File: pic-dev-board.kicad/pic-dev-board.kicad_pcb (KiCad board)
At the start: 2 copper layers, 100 x 100 mm, 80 parts, among them J1 Conn_GP0, J10 Jumper DATin, J11 Conn_SR_2, J12 Conn_SR_1, J13 Conn_5V_GND, J14 Jumper CLKin, J15 Barrel_Jack_Switch, J16 RUN/~PGM, J17 I2C, J18 GP1(RA1)/RB6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

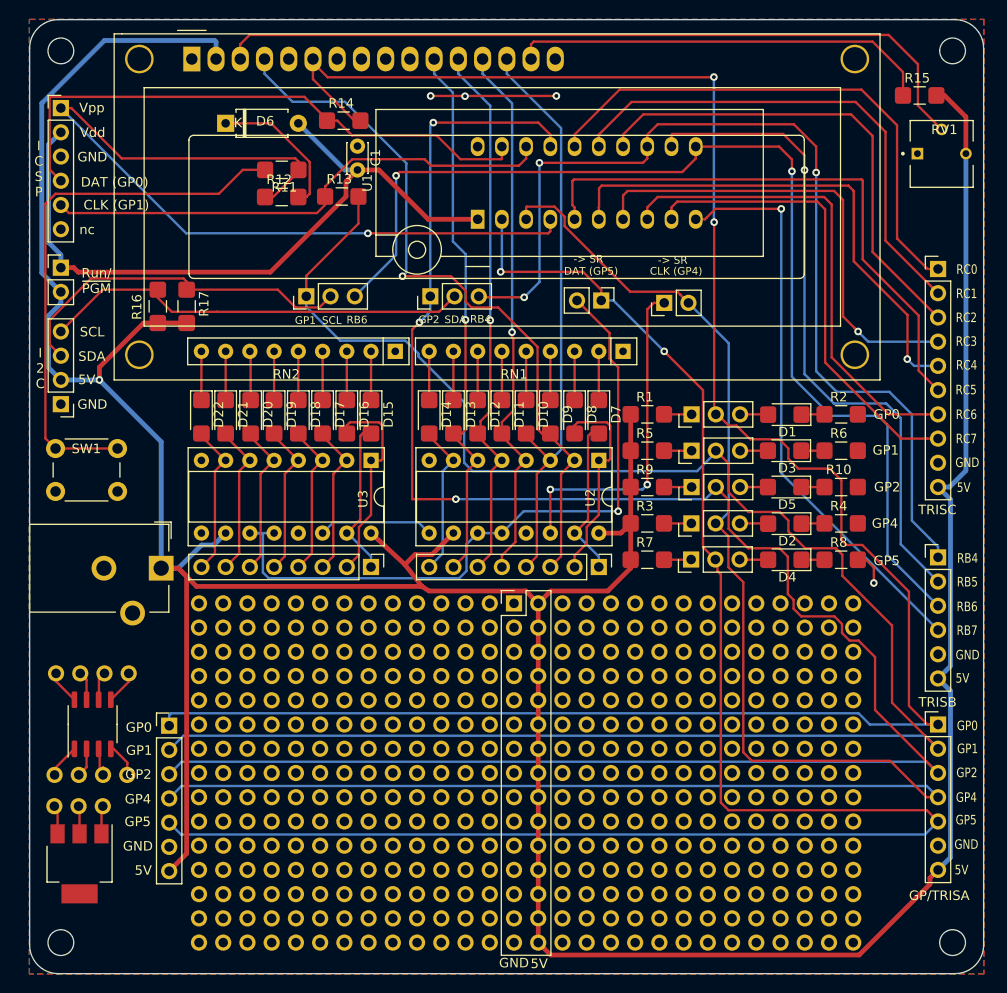
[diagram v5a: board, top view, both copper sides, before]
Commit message: fine-tuning of traces
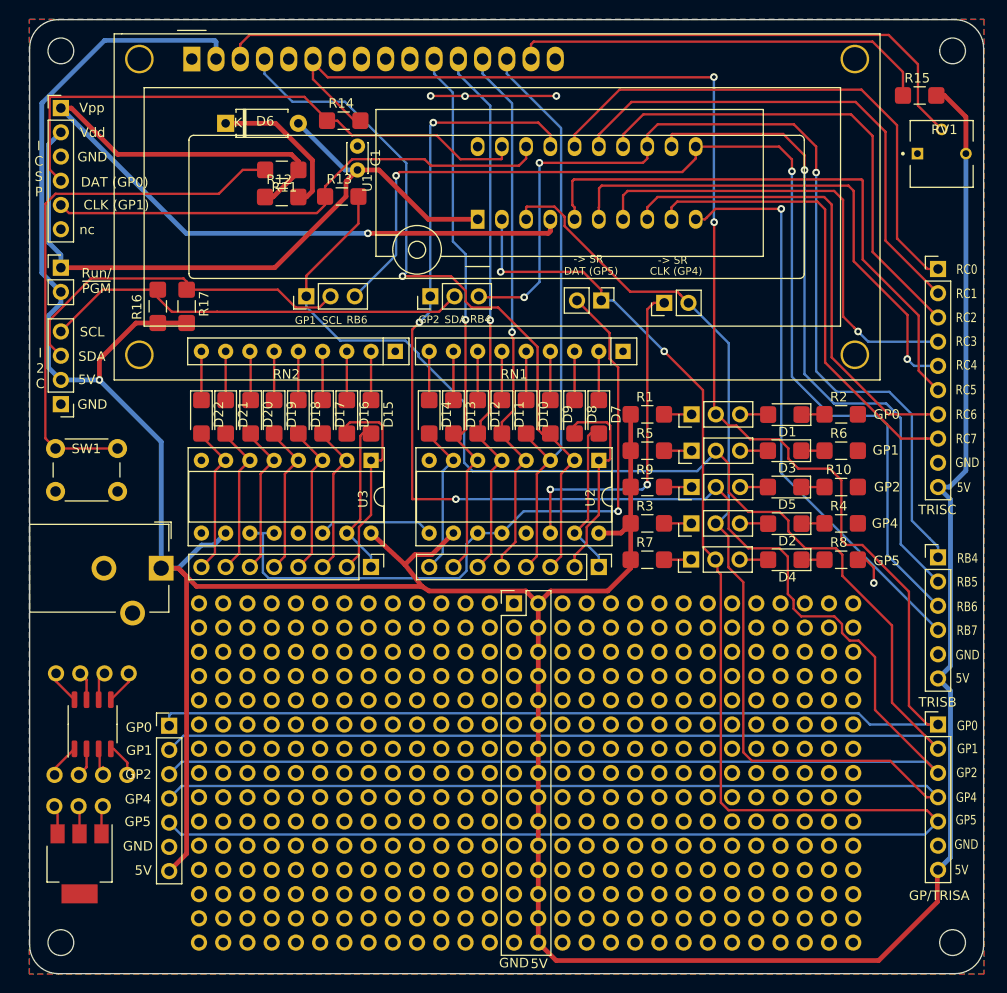
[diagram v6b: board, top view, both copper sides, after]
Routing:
- net +5V: track 389.5 -> 392.0 mm
- net Net-(D6-Pad1): track 15.2 -> 15.7 mm
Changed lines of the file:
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@@
     (thickness 1.6)
     (drawings 73)
-    (tracks 691)
+    (tracks 688)
     (zones 0)
     (modules 80)
@@
     (add_net "Net-(D5-Pad1)")
     (add_net "Net-(D5-Pad2)")
-    (add_net "Net-(D6-Pad1)")
     (add_net "Net-(D7-Pad1)")
     (add_net "Net-(D8-Pad1)")
@@
     (add_net +5V)
     (add_net /Vdd)
+    (add_net "Net-(D6-Pad1)")
   )
   (module Socket:DIP_Socket-20_W4.3_W5.08_W7.62_W10.16_W10.9_3M_220-3342-00-0602J (layer F.Cu)
@@
   (segment (start 31.973999 43.108401) (end 31.973999 53.349999) (width 0.5) (layer B.Cu) (net 1))
   (segment (start 33.274 41.8084) (end 31.973999 43.108401) (width 0.5) (layer B.Cu) (net 1) (status 10))
-  (segment (start 63.16609 46.95371) (end 63.563601 46.556199) (width 0.5) (layer F.Cu) (net 1))
-  (segment (start 34.624 56) (end 35.092001 56.468001) (width 0.5) (layer F.Cu) (net 1))
-  (segment (start 33.274 56) (end 34.624 56) (width 0.5) (layer F.Cu) (net 1))
-  (segment (start 63.563601 46.556199) (end 64.3636 45.7562) (width 0.5) (layer F.Cu) (net 1))
-  (segment (start 55.229639 56.468001) (end 63.16609 48.53155) (width 0.5) (layer F.Cu) (net 1))
-  (segment (start 63.16609 48.53155) (end 63.16609 46.95371) (width 0.5) (layer F.Cu) (net 1))
-  (segment (start 35.092001 56.468001) (end 55.229639 56.468001) (width 0.5) (layer F.Cu) (net 1))
   (segment (start 63.0536 45.7562) (end 64.3636 45.7562) (width 0.5) (layer B.Cu) (net 1))
   (segment (start 58.166 40.8686) (end 63.0536 45.7562) (width 0.5) (layer B.Cu) (net 1))
@@
   (segment (start 64.3636 45.7562) (end 66.6096 45.7562) (width 0.5) (layer F.Cu) (net 1))
   (segment (start 66.6096 45.7562) (end 71.7804 50.927) (width 0.5) (layer F.Cu) (net 1))
+  (segment (start 63.563601 46.556199) (end 64.3636 45.7562) (width 0.5) (layer F.Cu) (net 1))
+  (segment (start 63.16609 46.95371) (end 63.563601 46.556199) (width 0.5) (layer F.Cu) (net 1))
+  (segment (start 63.16609 48.53155) (end 63.16609 46.95371) (width 0.5) (layer F.Cu) (net 1))
+  (segment (start 33.274 56) (end 55.69764 56) (width 0.5) (layer F.Cu) (net 1))
+  (segment (start 55.69764 56) (end 63.16609 48.53155) (width 0.5) (layer F.Cu) (net 1))
   (via (at 118.491 89.0524) (size 0.8) (drill 0.4) (layers F.Cu B.Cu) (net 2))
   (segment (start 118.491 87.4395) (end 118.491 89.0524) (width 0.25) (layer F.Cu) (net 2))
@@
   (segment (start 104.648 78.994) (end 107.2125 78.994) (width 0.25) (layer F.Cu) (net 11) (status 30))
   (segment (start 110.7075 78.994) (end 113.3205 78.994) (width 0.25) (layer F.Cu) (net 12) (status 30))
-  (segment (start 55.313864 40.8686) (end 51.696 40.8686) (width 0.25) (layer F.Cu) (net 13))
-  (segment (start 51.696 40.8686) (end 50.546 40.8686) (width 0.25) (layer F.Cu) (net 13))
-  (segment (start 59.35531 44.910046) (end 55.313864 40.8686) (width 0.25) (layer F.Cu) (net 13))
-  (segment (start 59.35531 48.25179) (end 59.35531 44.910046) (width 0.25) (layer F.Cu) (net 13))
-  (segment (start 59.0169 48.5902) (end 59.35531 48.25179) (width 0.25) (layer F.Cu) (net 13))
-  (segment (start 58.1669 48.5902) (end 59.0169 48.5902) (width 0.25) (layer F.Cu) (net 13))
+  (segment (start 59.0169 48.5902) (end 58.1669 48.5902) (width 0.5) (layer F.Cu) (net 13))
+  (segment (start 59.6392 44.7294) (end 59.6392 47.9679) (width 0.5) (layer F.Cu) (net 13))
+  (segment (start 59.6392 47.9679) (end 59.0169 48.5902) (width 0.5) (layer F.Cu) (net 13))
+  (segment (start 55.7784 40.8686) (end 59.6392 44.7294) (width 0.5) (layer F.Cu) (net 13))
+  (segment (start 50.546 40.8686) (end 55.7784 40.8686) (width 0.5) (layer F.Cu) (net 13))
   (segment (start 88.536999 73.631501) (end 88.787 73.3815) (width 0.25) (layer F.Cu) (net 14) (status 20))
   (segment (start 88.536999 82.405001) (end 88.536999 73.631501) (width 0.25) (layer F.Cu) (net 14))
@@
   (segment (start 126.522001 100.360001) (end 126.522001 117.825999) (width 0.5) (layer B.Cu) (net 53))
   (segment (start 125.222 99.06) (end 126.522001 100.360001) (width 0.5) (layer B.Cu) (net 53) (status 10))
-  (segment (start 84.612001 128.046001) (end 83.312 126.746) (width 0.5) (layer F.Cu) (net 53) (status 20))
-  (segment (start 116.956001 128.046001) (end 84.612001 128.046001) (width 0.5) (layer F.Cu) (net 53))
-  (segment (start 124.372001 120.630001) (end 116.956001 128.046001) (width 0.5) (layer F.Cu) (net 53))
-  (segment (start 124.372001 119.975999) (end 124.372001 120.630001) (width 0.5) (layer F.Cu) (net 53))
-  (segment (start 125.222 119.126) (end 124.372001 119.975999) (width 0.5) (layer F.Cu) (net 53) (status 10))
   (segment (start 83.312 126.746) (end 83.312 124.206) (width 0.5) (layer F.Cu) (net 53) (status 30))
   (segment (start 83.312 124.206) (end 83.312 91.186) (width 0.5) (layer F.Cu) (net 53) (status 30))
@@
   (segment (start 43.7896 74.2442) (end 37.3126 67.7672) (width 0.5) (layer B.Cu) (net 53))
   (via (at 37.3126 67.7672) (size 0.8) (drill 0.4) (layers F.Cu B.Cu) (net 53))
-  (segment (start 37.3126 66.430598) (end 37.3126 67.7672) (width 0.5) (layer F.Cu) (net 53))
-  (segment (start 41.944098 61.7991) (end 37.3126 66.430598) (width 0.5) (layer F.Cu) (net 53))
-  (segment (start 43.434 61.7991) (end 41.944098 61.7991) (width 0.5) (layer F.Cu) (net 53) (status 10))
   (segment (start 43.434 61.7991) (end 46.4566 61.7991) (width 0.5) (layer F.Cu) (net 53) (status 30))
   (segment (start 46.451999 88.365399) (end 45.5896 87.503) (width 0.5) (layer F.Cu) (net 53))
@@
   (segment (start 45.5896 87.503) (end 43.7896 87.503) (width 0.5) (layer F.Cu) (net 53) (status 20))
   (segment (start 44.6278 119.253) (end 46.451999 117.428801) (width 0.5) (layer F.Cu) (net 53) (status 10))
+  (segment (start 37.3126 65.6336) (end 37.3126 67.7672) (width 0.5) (layer F.Cu) (net 53))
+  (segment (start 43.434 61.7991) (end 41.1471 61.7991) (width 0.5) (layer F.Cu) (net 53))
+  (segment (start 41.1471 61.7991) (end 37.3126 65.6336) (width 0.5) (layer F.Cu) (net 53))
+  (segment (start 85.1916 128.6256) (end 83.312 126.746) (width 0.5) (layer F.Cu) (net 53))
+  (segment (start 118.999 128.6256) (end 85.1916 128.6256) (width 0.5) (layer F.Cu) (net 53))
+  (segment (start 125.1458 122.4788) (end 118.999 128.6256) (width 0.5) (layer F.Cu) (net 53))
+  (segment (start 125.222 119.126) (end 125.1458 119.2022) (width 0.5) (layer F.Cu) (net 53))
+  (segment (start 125.1458 119.2022) (end 125.1458 122.4788) (width 0.5) (layer F.Cu) (net 53))
   (segment (start 99.568 71.374) (end 96.4955 71.374) (width 0.25) (layer F.Cu) (net 54) (status 30))
   (segment (start 105.702998 107.696) (end 104.807001 106.800003) (width 0.25) (layer F.Cu) (net 55))
@@
   (segment (start 33.274 46.8884) (end 32.098999 45.713399) (width 0.25) (layer F.Cu) (net 65))
   (segment (start 79.42699 44.63201) (end 79.502 44.557) (width 0.25) (layer F.Cu) (net 65))
-  (segment (start 58.1803 45.9318) (end 58.1803 45.7454) (width 0.25) (layer F.Cu) (net 66))
-  (segment (start 55.5219 48.5902) (end 58.1803 45.9318) (width 0.25) (layer F.Cu) (net 66))
-  (segment (start 54.6719 48.5902) (end 55.5219 48.5902) (width 0.25) (layer F.Cu) (net 66))
-  (segment (start 58.1803 44.8704) (end 58.1803 45.7454) (width 0.25) (layer F.Cu) (net 66))
-  (segment (start 34.374 39.2684) (end 39.65099 44.54539) (width 0.25) (layer F.Cu) (net 66))
-  (segment (start 57.85529 44.54539) (end 58.1803 44.8704) (width 0.25) (layer F.Cu) (net 66))
-  (segment (start 39.65099 44.54539) (end 57.85529 44.54539) (width 0.25) (layer F.Cu) (net 66))
-  (segment (start 33.274 39.2684) (end 34.374 39.2684) (width 0.25) (layer F.Cu) (net 66))
-  (segment (start 84.3588 52.4002) (end 65.4558 52.4002) (width 0.25) (layer F.Cu) (net 66))
-  (segment (start 84.582 50.927) (end 84.582 52.177) (width 0.25) (layer F.Cu) (net 66))
+  (segment (start 58.1803 45.9318) (end 58.1803 45.7454) (width 0.5) (layer F.Cu) (net 66))
+  (segment (start 55.5219 48.5902) (end 58.1803 45.9318) (width 0.5) (layer F.Cu) (net 66))
+  (segment (start 54.6719 48.5902) (end 55.5219 48.5902) (width 0.5) (layer F.Cu) (net 66))
+  (segment (start 84.3588 52.4002) (end 65.4558 52.4002) (width 0.5) (layer F.Cu) (net 66))
+  (segment (start 84.582 50.927) (end 84.582 52.177) (width 0.5) (layer F.Cu) (net 66))
   (via (at 65.4558 52.4002) (size 0.8) (drill 0.4) (layers F.Cu B.Cu) (net 66))
-  (segment (start 84.582 52.177) (end 84.3588 52.4002) (width 0.25) (layer F.Cu) (net 66))
-  (segment (start 46.4058 52.4002) (end 33.274 39.2684) (width 0.25) (layer B.Cu) (net 66))
-  (segment (start 65.4558 52.4002) (end 46.4058 52.4002) (width 0.25) (layer B.Cu) (net 66))
+  (segment (start 84.582 52.177) (end 84.3588 52.4002) (width 0.5) (layer F.Cu) (net 66))
+  (segment (start 46.4058 52.4002) (end 33.274 39.2684) (width 0.5) (layer B.Cu) (net 66))
+  (segment (start 65.4558 52.4002) (end 46.4058 52.4002) (width 0.5) (layer B.Cu) (net 66))
+  (segment (start 57.4297 44.1198) (end 58.1803 44.8704) (width 0.5) (layer F.Cu) (net 66))
+  (segment (start 58.1803 44.8704) (end 58.1803 45.7454) (width 0.5) (layer F.Cu) (net 66))
+  (segment (start 39.2254 44.1198) (end 57.4297 44.1198) (width 0.5) (layer F.Cu) (net 66))
+  (segment (start 33.274 39.2684) (end 34.374 39.2684) (width 0.5) (layer F.Cu) (net 66))
+  (segment (start 34.374 39.2684) (end 39.2254 44.1198) (width 0.5) (layer F.Cu) (net 66))
   (segment (start 124.019919 73.914) (end 125.222 73.914) (width 0.25) (layer F.Cu) (net 67))
   (segment (start 121.365864 73.914) (end 124.019919 73.914) (width 0.25) (layer F.Cu) (net 67))

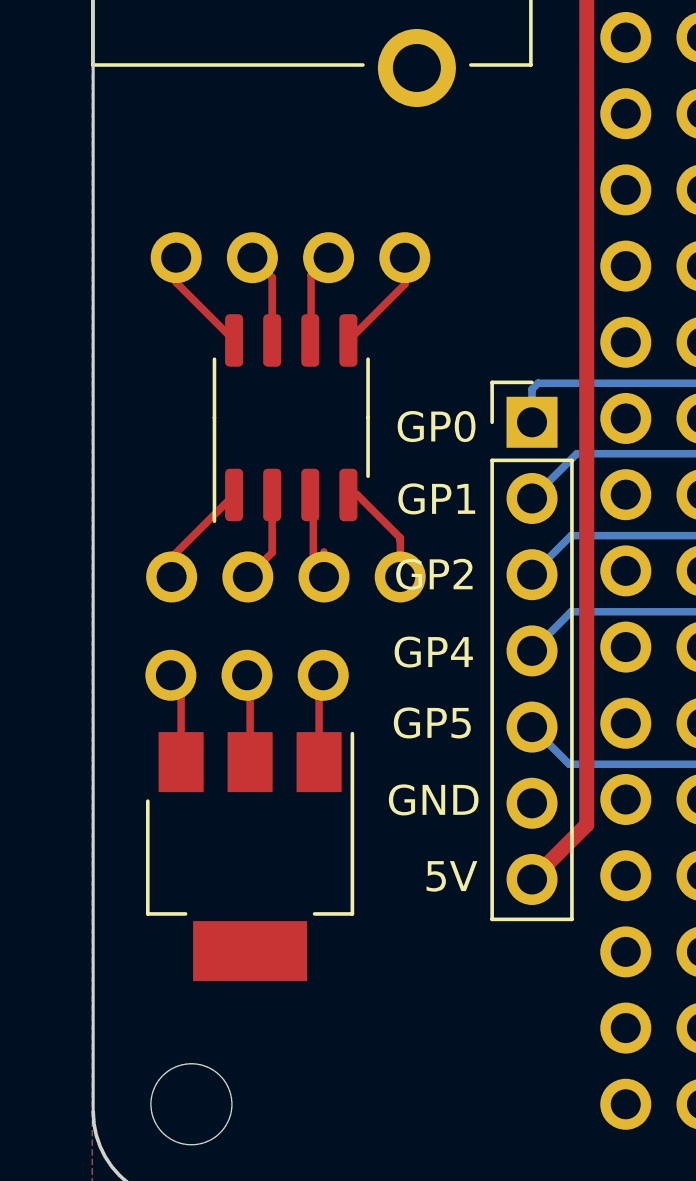
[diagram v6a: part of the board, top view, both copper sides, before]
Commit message: Rev4: added SO-8/SOT-223 components to schema to prevent DRC-errors on pcb
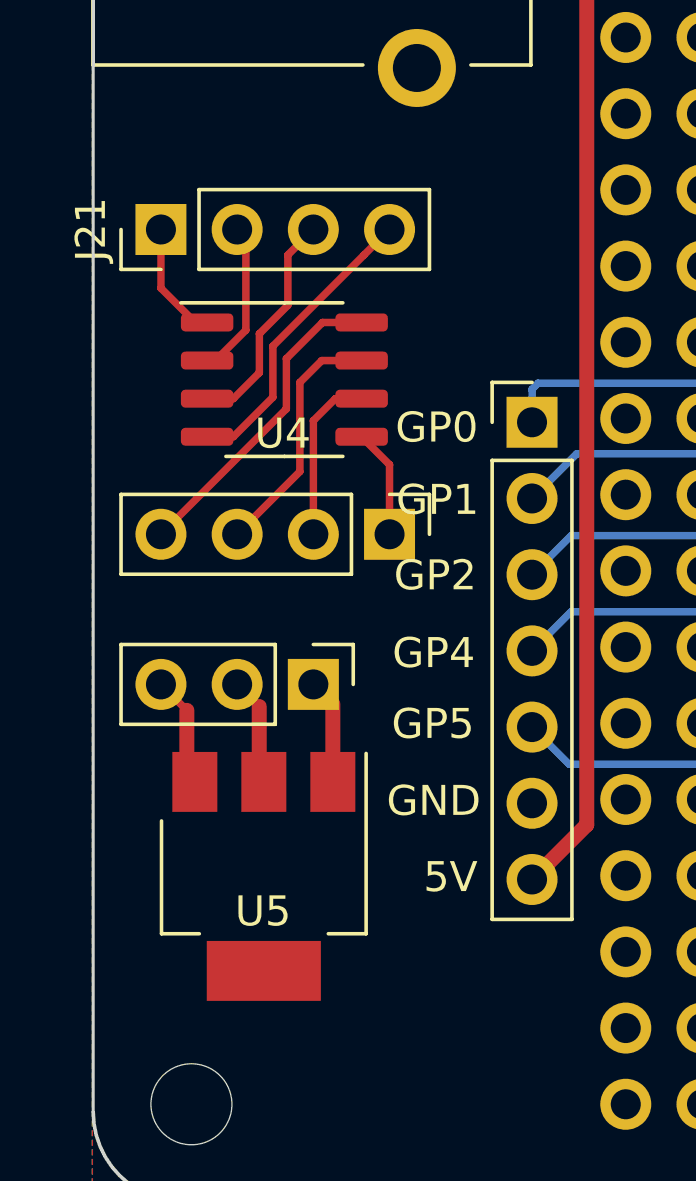
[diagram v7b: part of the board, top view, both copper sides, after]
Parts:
- removed the REF** at (37.7, 112.4)
- removed the REF** at (35.2, 118.5)
- removed the REF** at (32.6, 109.2)
- removed the REF** at (32.8, 98.5)
- removed the REF** at (36.6, 103.9)
- added J21: Conn_01x04_Male, Connector_PinHeader_2.54mm:PinHeader_1x04_P2.54mm_Vertical, F.Cu at (32.3, 97.6)
- added J22: Conn_01x04_Male, Connector_PinHeader_2.54mm:PinHeader_1x04_P2.54mm_Vertical, F.Cu at (39.9, 107.7)
- added J23: Conn_01x03_Male, Connector_PinHeader_2.54mm:PinHeader_1x03_P2.54mm_Vertical, F.Cu at (37.3, 112.8)
- added U4: SO-8-ProtoArea, Package_SO:SO-8_3.9x4.9mm_P1.27mm, F.Cu at (36.4, 102.6)
- added U5: SOT-223-ProtoArea, Package_TO_SOT_SMD:SOT-223, F.Cu at (35.7, 119.2)
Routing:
- net (no net): track 37.6 -> 0.00 mm
- net Net-(J22-Pad4): track 0.00 -> 10.6 mm
- net Net-(J21-Pad4): track 0.00 -> 9.94 mm
- net Net-(J22-Pad3): track 0.00 -> 8.29 mm
- net Net-(J21-Pad3): track 0.00 -> 7.62 mm
- net Net-(J22-Pad2): track 0.00 -> 5.70 mm
- net Net-(J21-Pad2): track 0.00 -> 5.19 mm
- net Net-(J21-Pad1): track 0.00 -> 3.97 mm
- net Net-(J23-Pad3): track 0.00 -> 3.72 mm
- net Net-(J22-Pad1): track 0.00 -> 3.64 mm
- net Net-(J23-Pad2): track 0.00 -> 3.62 mm
- net Net-(J23-Pad1): track 0.00 -> 3.52 mm
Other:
- board text added: "Rev 4"
- board text removed: "Rev 2"

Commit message: fine-tuning of labels
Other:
- board text added: "1"
- board text added: "2"
- board text added: "4"
- board text added: "8"
- board text added: "D15 - D22"
- board text added: "D7 - D14"
- board text added: "PIC12Fxxx"
- board text added: "PIC16Fxxx"
- board text added: "Reset"
- board text added: "SN74HC595"
